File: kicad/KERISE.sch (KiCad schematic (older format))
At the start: 20 parts, among them P1 ANT, SW1 SW_Push, U1 FLASH, U2 ESP32, U3 XTAL

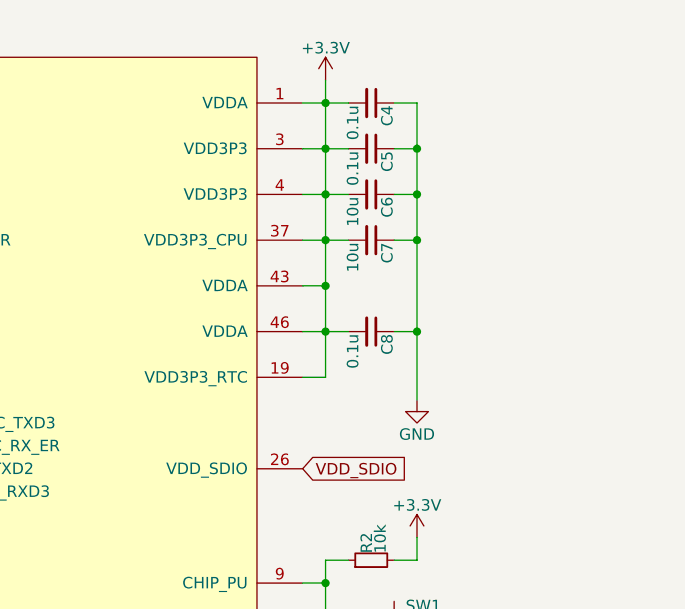
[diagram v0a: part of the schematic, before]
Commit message: フットプリントを改良，アナログ電源を分離
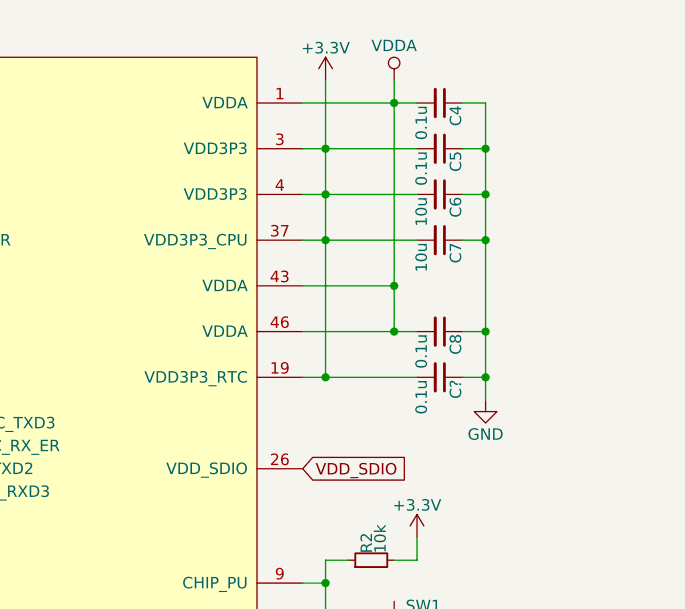
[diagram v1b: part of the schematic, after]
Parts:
- added C?: 0.1u, Capacitors_SMD:C_0201, symbol C_Small
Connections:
- net +3V3: now also C?.2; no longer C4.2, C8.2, U2.1 (VDDA), U2.43 (VDDA), U2.46 (VDDA)
- net GND: now also C?.1
- new net VDDA: C4.2, C8.2, U2.1 (VDDA), U2.43 (VDDA), U2.46 (VDDA)
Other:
- moved on the sheet: C4, C5, C6, C7, C8
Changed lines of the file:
@@
 L C_Small C8
 U 1 1 5894E774
-P 8800 2000
-F 0 "C8" H 8810 2070 50  0000 L CNN
-F 1 "0.1u" H 8810 1920 50  0000 L CNN
-F 2 "Capacitors_SMD:C_0201" H 8800 2000 50  0001 C CNN
-F 3 "" H 8800 2000 50  0000 C CNN
-	1    8800 2000
+P 9100 2000
+F 0 "C8" H 9110 2070 50  0000 L CNN
+F 1 "0.1u" H 9110 1920 50  0000 L CNN
+F 2 "Capacitors_SMD:C_0201" H 9100 2000 50  0001 C CNN
+F 3 "" H 9100 2000 50  0000 C CNN
+	1    9100 2000
 	0    1    1    0
 $EndComp
@@
 L GND #PWR04
 U 1 1 58A70C45
-P 9000 2300
-F 0 "#PWR04" H 9000 2050 50  0001 C CNN
-F 1 "GND" H 9000 2150 50  0000 C CNN
-F 2 "" H 9000 2300 50  0000 C CNN
-F 3 "" H 9000 2300 50  0000 C CNN
-	1    9000 2300
+P 9300 2300
+F 0 "#PWR04" H 9300 2050 50  0001 C CNN
+F 1 "GND" H 9300 2150 50  0000 C CNN
+F 2 "" H 9300 2300 50  0000 C CNN
+F 3 "" H 9300 2300 50  0000 C CNN
+	1    9300 2300
 	1    0    0    -1
 $EndComp
@@
 L C_Small C6
 U 1 1 58A9401A
-P 8800 1400
-F 0 "C6" H 8810 1470 50  0000 L CNN
-F 1 "10u" H 8810 1320 50  0000 L CNN
-F 2 "Capacitors_SMD:C_0402" H 8800 1400 50  0001 C CNN
-F 3 "" H 8800 1400 50  0000 C CNN
-	1    8800 1400
+P 9100 1400
+F 0 "C6" H 9110 1470 50  0000 L CNN
+F 1 "10u" H 9110 1320 50  0000 L CNN
+F 2 "Capacitors_SMD:C_0402" H 9100 1400 50  0001 C CNN
+F 3 "" H 9100 1400 50  0000 C CNN
+	1    9100 1400
 	0    1    1    0
 $EndComp
@@
 L C_Small C5
 U 1 1 58A94440
-P 8800 1200
-F 0 "C5" H 8810 1270 50  0000 L CNN
-F 1 "0.1u" H 8810 1120 50  0000 L CNN
-F 2 "Capacitors_SMD:C_0201" H 8800 1200 50  0001 C CNN
-F 3 "" H 8800 1200 50  0000 C CNN
-	1    8800 1200
+P 9100 1200
+F 0 "C5" H 9110 1270 50  0000 L CNN
+F 1 "0.1u" H 9110 1120 50  0000 L CNN
+F 2 "Capacitors_SMD:C_0201" H 9100 1200 50  0001 C CNN
+F 3 "" H 9100 1200 50  0000 C CNN
+	1    9100 1200
 	0    1    1    0
 $EndComp
@@
 L C_Small C7
 U 1 1 58AFD8EC
-P 8800 1600
-F 0 "C7" H 8810 1670 50  0000 L CNN
-F 1 "10u" H 8810 1520 50  0000 L CNN
-F 2 "Capacitors_SMD:C_0402" H 8800 1600 50  0001 C CNN
-F 3 "" H 8800 1600 50  0000 C CNN
-	1    8800 1600
+P 9100 1600
+F 0 "C7" H 9110 1670 50  0000 L CNN
+F 1 "10u" H 9110 1520 50  0000 L CNN
+F 2 "Capacitors_SMD:C_0402" H 9100 1600 50  0001 C CNN
+F 3 "" H 9100 1600 50  0000 C CNN
+	1    9100 1600
 	0    1    1    0
 $EndComp
@@
 Wire Wire Line
 	8600 3100 8500 3100
-Connection ~ 9000 2000
-Wire Wire Line
-	8900 2000 9000 2000
-Wire Wire Line
-	8600 1800 8500 1800
-Wire Wire Line
-	9000 1000 9000 2300
-Wire Wire Line
-	8500 1000 8700 1000
-Connection ~ 8600 2000
-Wire Wire Line
-	8500 2000 8700 2000
-Wire Wire Line
-	8600 2200 8500 2200
+Connection ~ 9300 2000
+Wire Wire Line
+	9200 2000 9300 2000
+Wire Wire Line
+	8500 1800 8900 1800
+Wire Wire Line
+	9300 1000 9300 2300
+Wire Wire Line
+	8500 1000 9000 1000
+Wire Wire Line
+	8500 2000 9000 2000
+Wire Wire Line
+	8500 2200 9000 2200
 Wire Wire Line
 	10000 4600 10000 5000
@@
 Wire Wire Line
 	4400 5700 4400 5800
-Connection ~ 9000 1400
-Wire Wire Line
-	9000 1400 8900 1400
-Wire Wire Line
-	8900 1200 9000 1200
+Connection ~ 9300 1400
+Wire Wire Line
+	9300 1400 9200 1400
+Wire Wire Line
+	9200 1200 9300 1200
 Wire Wire Line
 	9000 3000 8900 3000
@@
 Wire Wire Line
 	8700 3700 8700 3800
-Connection ~ 8600 1000
-Connection ~ 9000 1600
-Wire Wire Line
-	9000 1600 8900 1600
-Connection ~ 8600 1800
+Connection ~ 9300 1600
+Wire Wire Line
+	9300 1600 9200 1600
 Connection ~ 8600 1600
 Connection ~ 8600 1400
 Wire Wire Line
-	8500 1600 8700 1600
+	8500 1600 9000 1600
 Connection ~ 8600 1200
 Wire Wire Line
-	8500 1400 8700 1400
-Wire Wire Line
-	8500 1200 8700 1200
+	8500 1400 9000 1400
+Wire Wire Line
+	8500 1200 9000 1200
 Wire Wire Line
 	2600 5100 2500 5100
@@
 L C_Small C4
 U 1 1 593708F9
-P 8800 1000
-F 0 "C4" H 8810 1070 50  0000 L CNN
-F 1 "0.1u" H 8810 920 50  0000 L CNN
-F 2 "Capacitors_SMD:C_0201" H 8800 1000 50  0001 C CNN
-F 3 "" H 8800 1000 50  0000 C CNN
-	1    8800 1000
+P 9100 1000
+F 0 "C4" H 9110 1070 50  0000 L CNN
+F 1 "0.1u" H 9110 920 50  0000 L CNN
+F 2 "Capacitors_SMD:C_0201" H 9100 1000 50  0001 C CNN
+F 3 "" H 9100 1000 50  0000 C CNN
+	1    9100 1000
 	0    1    1    0
 $EndComp
 Wire Wire Line
-	8900 1000 9000 1000
-Connection ~ 9000 1200
+	9200 1000 9300 1000
+Connection ~ 9300 1200
 $Comp
 L ESP32 U2
@@
 Wire Wire Line
 	1400 1600 1500 1600
+$Comp
+L VDDA #PWR?
+U 1 1 59C3BA09
+P 8900 900
+F 0 "#PWR?" H 8900 750 50  0001 C CNN
+F 1 "VDDA" H 8900 1050 50  0000 C CNN
+F 2 "" H 8900 900 50  0001 C CNN
+F 3 "" H 8900 900 50  0001 C CNN
+	1    8900 900
+	1    0    0    -1
+$EndComp
+Wire Wire Line
+	8900 900  8900 2000
+Connection ~ 8900 2000
+Connection ~ 8900 1000
+Connection ~ 8900 1800
+$Comp
+L C_Small C?
+U 1 1 59C3D339
+P 9100 2200
+F 0 "C?" H 9110 2270 50  0000 L CNN
+F 1 "0.1u" H 9110 2120 50  0000 L CNN
+F 2 "Capacitors_SMD:C_0201" H 9100 2200 50  0001 C CNN
+F 3 "" H 9100 2200 50  0000 C CNN
+	1    9100 2200
+	0    1    1    0
+$EndComp
+Wire Wire Line
+	9200 2200 9300 2200
+Connection ~ 9300 2200
+Connection ~ 8600 2200
 $EndSCHEMATC

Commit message: 回路とフットプリントを改良
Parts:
- removed C?: 0.1u, Capacitors_SMD:C_0201, symbol C_Small
- renumbered C7 to C10, C8 to C11, C12 to C13, C9 to C4, C10 to C5, C11 to C6, C4 to C7, C5 to C8, C6 to C9
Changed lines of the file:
@@
 Main
 $Comp
-L C_Small C8
+L C_Small C11
 U 1 1 5894E774
 P 9100 2000
-F 0 "C8" H 9110 2070 50  0000 L CNN
+F 0 "C11" H 9110 2070 50  0000 L CNN
 F 1 "0.1u" H 9110 1920 50  0000 L CNN
 F 2 "Capacitors_SMD:C_0201" H 9100 2000 50  0001 C CNN
@@
 $EndComp
 $Comp
-L C_Small C10
+L C_Small C5
 U 1 1 58A71512
 P 9000 3900
-F 0 "C10" H 9010 3970 50  0000 L CNN
+F 0 "C5" H 9010 3970 50  0000 L CNN
 F 1 "3.3n" H 9010 3820 50  0000 L CNN
 F 2 "Capacitors_SMD:C_0201" H 9000 3900 50  0001 C CNN
@@
 $EndComp
 $Comp
-L C_Small C12
+L C_Small C13
 U 1 1 58A770D7
 P 9300 3900
-F 0 "C12" H 9310 3970 50  0000 L CNN
+F 0 "C13" H 9310 3970 50  0000 L CNN
 F 1 "0.01u" H 9310 3820 50  0000 L CNN
 F 2 "Capacitors_SMD:C_0201" H 9300 3900 50  0001 C CNN
@@
 $EndComp
 $Comp
-L C_Small C6
+L C_Small C9
 U 1 1 58A9401A
 P 9100 1400
-F 0 "C6" H 9110 1470 50  0000 L CNN
+F 0 "C9" H 9110 1470 50  0000 L CNN
 F 1 "10u" H 9110 1320 50  0000 L CNN
 F 2 "Capacitors_SMD:C_0402" H 9100 1400 50  0001 C CNN
@@
 $EndComp
 $Comp
-L C_Small C5
+L C_Small C8
 U 1 1 58A94440
 P 9100 1200
-F 0 "C5" H 9110 1270 50  0000 L CNN
+F 0 "C8" H 9110 1270 50  0000 L CNN
 F 1 "0.1u" H 9110 1120 50  0000 L CNN
 F 2 "Capacitors_SMD:C_0201" H 9100 1200 50  0001 C CNN
@@
 $EndComp
 $Comp
-L C_Small C11
+L C_Small C6
 U 1 1 58ADFB26
 P 9000 4800
-F 0 "C11" H 9010 4870 50  0000 L CNN
+F 0 "C6" H 9010 4870 50  0000 L CNN
 F 1 "22p" H 9010 4720 50  0000 L CNN
 F 2 "Capacitors_SMD:C_0201" H 9000 4800 50  0001 C CNN
@@
 $EndComp
 $Comp
-L C_Small C9
+L C_Small C4
 U 1 1 58ADFC50
 P 8800 4800
-F 0 "C9" H 8810 4870 50  0000 L CNN
+F 0 "C4" H 8810 4870 50  0000 L CNN
 F 1 "22p" H 8810 4720 50  0000 L CNN
 F 2 "Capacitors_SMD:C_0201" H 8800 4800 50  0001 C CNN
@@
 $EndComp
 $Comp
-L C_Small C7
+L C_Small C10
 U 1 1 58AFD8EC
 P 9100 1600
-F 0 "C7" H 9110 1670 50  0000 L CNN
+F 0 "C10" H 9110 1670 50  0000 L CNN
 F 1 "10u" H 9110 1520 50  0000 L CNN
 F 2 "Capacitors_SMD:C_0402" H 9100 1600 50  0001 C CNN
@@
 Wire Wire Line
 	8500 2000 9000 2000
-Wire Wire Line
-	8500 2200 9000 2200
 Wire Wire Line
 	10000 4600 10000 5000
@@
 	4500 1000 4400 1000
 $Comp
-L C_Small C4
+L C_Small C7
 U 1 1 593708F9
 P 9100 1000
-F 0 "C4" H 9110 1070 50  0000 L CNN
+F 0 "C7" H 9110 1070 50  0000 L CNN
 F 1 "0.1u" H 9110 920 50  0000 L CNN
 F 2 "Capacitors_SMD:C_0201" H 9100 1000 50  0001 C CNN
@@
 	1400 1600 1500 1600
 $Comp
-L VDDA #PWR?
+L VDDA #PWR014
 U 1 1 59C3BA09
 P 8900 900
-F 0 "#PWR?" H 8900 750 50  0001 C CNN
+F 0 "#PWR014" H 8900 750 50  0001 C CNN
 F 1 "VDDA" H 8900 1050 50  0000 C CNN
 F 2 "" H 8900 900 50  0001 C CNN
@@
 Connection ~ 8900 1000
 Connection ~ 8900 1800
-$Comp
-L C_Small C?
-U 1 1 59C3D339
-P 9100 2200
-F 0 "C?" H 9110 2270 50  0000 L CNN
-F 1 "0.1u" H 9110 2120 50  0000 L CNN
-F 2 "Capacitors_SMD:C_0201" H 9100 2200 50  0001 C CNN
-F 3 "" H 9100 2200 50  0000 C CNN
-	1    9100 2200
-	0    1    1    0
-$EndComp
-Wire Wire Line
-	9200 2200 9300 2200
-Connection ~ 9300 2200
-Connection ~ 8600 2200
+Wire Wire Line
+	8600 2200 8500 2200
 $EndSCHEMATC
